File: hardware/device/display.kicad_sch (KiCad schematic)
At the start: 8 parts, among them U19 ER-TFT024IPS-3

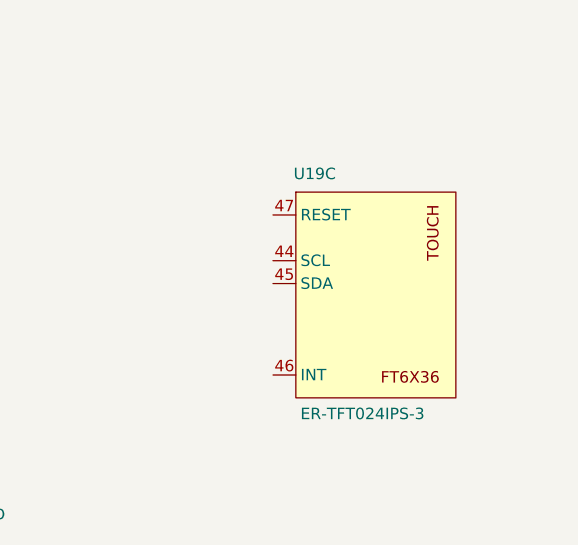
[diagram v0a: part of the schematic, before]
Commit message: feat: start codec layout
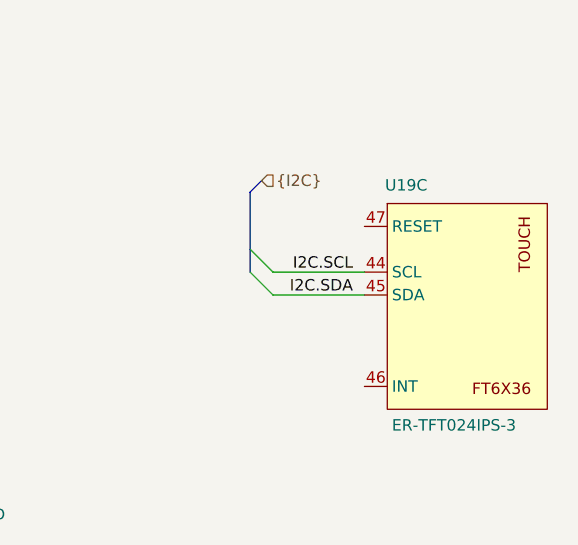
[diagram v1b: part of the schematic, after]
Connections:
- net I2C.SCL: now reaches U19.44 (SCL)
- net I2C.SDA: now reaches U19.45 (SDA)
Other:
- moved on the sheet: U19C
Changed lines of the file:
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@@
+	)
+	(bus_entry
+		(at 121.92 105.41)
+		(size -2.54 -2.54)
+		(stroke
+			(width 0)
+			(type default)
+		)
 	)
 	(bus_entry
@@
 	)
 	(bus_entry
+		(at 121.92 107.95)
+		(size -2.54 -2.54)
+		(stroke
+			(width 0)
+			(type default)
+		)
+	)
+	(bus_entry
 		(at 21.59 96.52)
 		(size -2.54 -2.54)
@@
 		)
 	)
+	(bus
+		(pts
+			(xy 119.38 96.52) (xy 119.38 102.87)
+		)
+		(stroke
+			(width 0)
+			(type default)
+		)
+	)
 	(wire
 		(pts
@@
 		)
 	)
+	(bus
+		(pts
+			(xy 119.38 102.87) (xy 119.38 105.41)
+		)
+		(stroke
+			(width 0)
+			(type default)
+		)
+	)
 	(wire
 		(pts
@@
 		)
 	)
+	(bus
+		(pts
+			(xy 119.38 96.52) (xy 120.65 95.25)
+		)
+		(stroke
+			(width 0)
+			(type default)
+		)
+	)
 	(wire
 		(pts
@@
 	(wire
 		(pts
+			(xy 121.92 105.41) (xy 132.08 105.41)
+		)
+		(stroke
+			(width 0)
+			(type default)
+		)
+	)
+	(wire
+		(pts
 			(xy 64.77 125.73) (xy 90.17 125.73)
 		)
@@
 		(pts
 			(xy 21.59 73.66) (xy 34.29 73.66)
+		)
+		(stroke
+			(width 0)
+			(type default)
+		)
+	)
+	(wire
+		(pts
+			(xy 121.92 107.95) (xy 132.08 107.95)
 		)
 		(stroke
@@
 		)
 	)
+	(label "I2C.SDA"
+		(at 130.81 107.95 180)
+		(effects
+			(font
+				(size 1.27 1.27)
+			)
+			(justify right bottom)
+		)
+	)
 	(label "FMC.D2"
 		(at 33.02 63.5 180)
@@
 		)
 	)
+	(label "I2C.SCL"
+		(at 130.81 105.41 180)
+		(effects
+			(font
+				(size 1.27 1.27)
+			)
+			(justify right bottom)
+		)
+	)
 	(label "FMC.NWE"
 		(at 33.02 111.76 180)
@@
 			)
 			(justify right bottom)
+		)
+	)
+	(hierarchical_label "{I2C}"
+		(shape input)
+		(at 120.65 95.25 0)
+		(effects
+			(font
+				(size 1.27 1.27)
+			)
+			(justify left)
 		)
 	)
@@
 	(symbol
 		(lib_id "pocket_synth:ER-TFT024IPS-3")
-		(at 133.35 107.95 0)
+		(at 143.51 109.22 0)
 		(unit 3)
 		(exclude_from_sim no)
@@
 		(dnp no)
 		(property "Reference" "U19"
-			(at 124.206 94.488 0)
+			(at 134.366 95.758 0)
 			(effects
 				(font
@@
 		)
 		(property "Value" "ER-TFT024IPS-3"
-			(at 124.968 121.158 0)
+			(at 135.128 122.428 0)
 			(effects
 				(font
@@
 		)
 		(property "Footprint" "pocket_synth:ER-TFT024IPS-3"
-			(at 133.35 107.95 0)
+			(at 143.51 109.22 0)
 			(effects
 				(font
@@
 		)
 		(property "Datasheet" ""
-			(at 133.35 107.95 0)
+			(at 143.51 109.22 0)
 			(effects
 				(font
@@
 		)
 		(property "Description" ""
-			(at 133.35 107.95 0)
+			(at 143.51 109.22 0)
 			(effects
 				(font
@@
 		)
 		(property "JLC" ""
-			(at 133.35 107.95 0)
-			(effects
-				(font
+			(at 143.51 109.22 0)
+			(effects
+				(font

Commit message: feat: various audio and power schematic layout
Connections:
- net GND: no longer U19.39 (TE)
- new net DISPLAY_TE: U19.39 (TE)
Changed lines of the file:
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@@
-	)
-	(junction
-		(at 90.17 93.98)
-		(diameter 0)
-		(color 0 0 0 0)
 	)
 	(junction
@@
 	(wire
 		(pts
-			(xy 90.17 77.47) (xy 90.17 93.98)
-		)
-		(stroke
-			(width 0)
-			(type default)
-		)
-	)
-	(wire
-		(pts
 			(xy 87.63 77.47) (xy 90.17 77.47)
 		)
@@
 	(wire
 		(pts
-			(xy 90.17 93.98) (xy 90.17 125.73)
+			(xy 90.17 77.47) (xy 90.17 125.73)
 		)
 		(stroke
@@
 	(wire
 		(pts
-			(xy 87.63 93.98) (xy 90.17 93.98)
+			(xy 87.63 93.98) (xy 92.71 93.98)
 		)
 		(stroke
@@
 		(effects
 			(font
+				(size 1.27 1.27)
+			)
+			(justify left)
+		)
+	)
+	(hierarchical_label "DISPLAY_TE"
+		(shape input)
+		(at 92.71 93.98 0)
+		(effects
+			(font

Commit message: chore: schematic organization
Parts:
- C4, C5, C6: footprint (none) -> Capacitor_SMD:C_0402_1005Metric
- R4, R5, R6, R7: footprint (none) -> Resistor_SMD:R_0402_1005Metric
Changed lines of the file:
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@@
 			)
 		)
-		(property "Footprint" ""
+		(property "Footprint" "Resistor_SMD:R_0402_1005Metric"
 			(at 115.57 61.468 90)
 			(effects
@@
 			)
 		)
-		(property "Footprint" ""
+		(property "Footprint" "Capacitor_SMD:C_0402_1005Metric"
 			(at 64.4652 35.56 0)
 			(effects
@@
 			)
 		)
-		(property "Footprint" ""
+		(property "Footprint" "Resistor_SMD:R_0402_1005Metric"
 			(at 115.57 57.658 90)
 			(effects
@@
 			)
 		)
-		(property "Footprint" ""
+		(property "Footprint" "Resistor_SMD:R_0402_1005Metric"
 			(at 115.57 65.278 90)
 			(effects
@@
 			)
 		)
-		(property "Footprint" ""
+		(property "Footprint" "Capacitor_SMD:C_0402_1005Metric"
 			(at 72.0852 35.56 0)
 			(effects
@@
 			)
 		)
-		(property "Footprint" ""
+		(property "Footprint" "Resistor_SMD:R_0402_1005Metric"
 			(at 115.57 69.088 90)
 			(effects
@@
 			)
 		)
-		(property "Footprint" ""
+		(property "Footprint" "Capacitor_SMD:C_0402_1005Metric"
 			(at 79.7052 35.56 0)
 			(effects

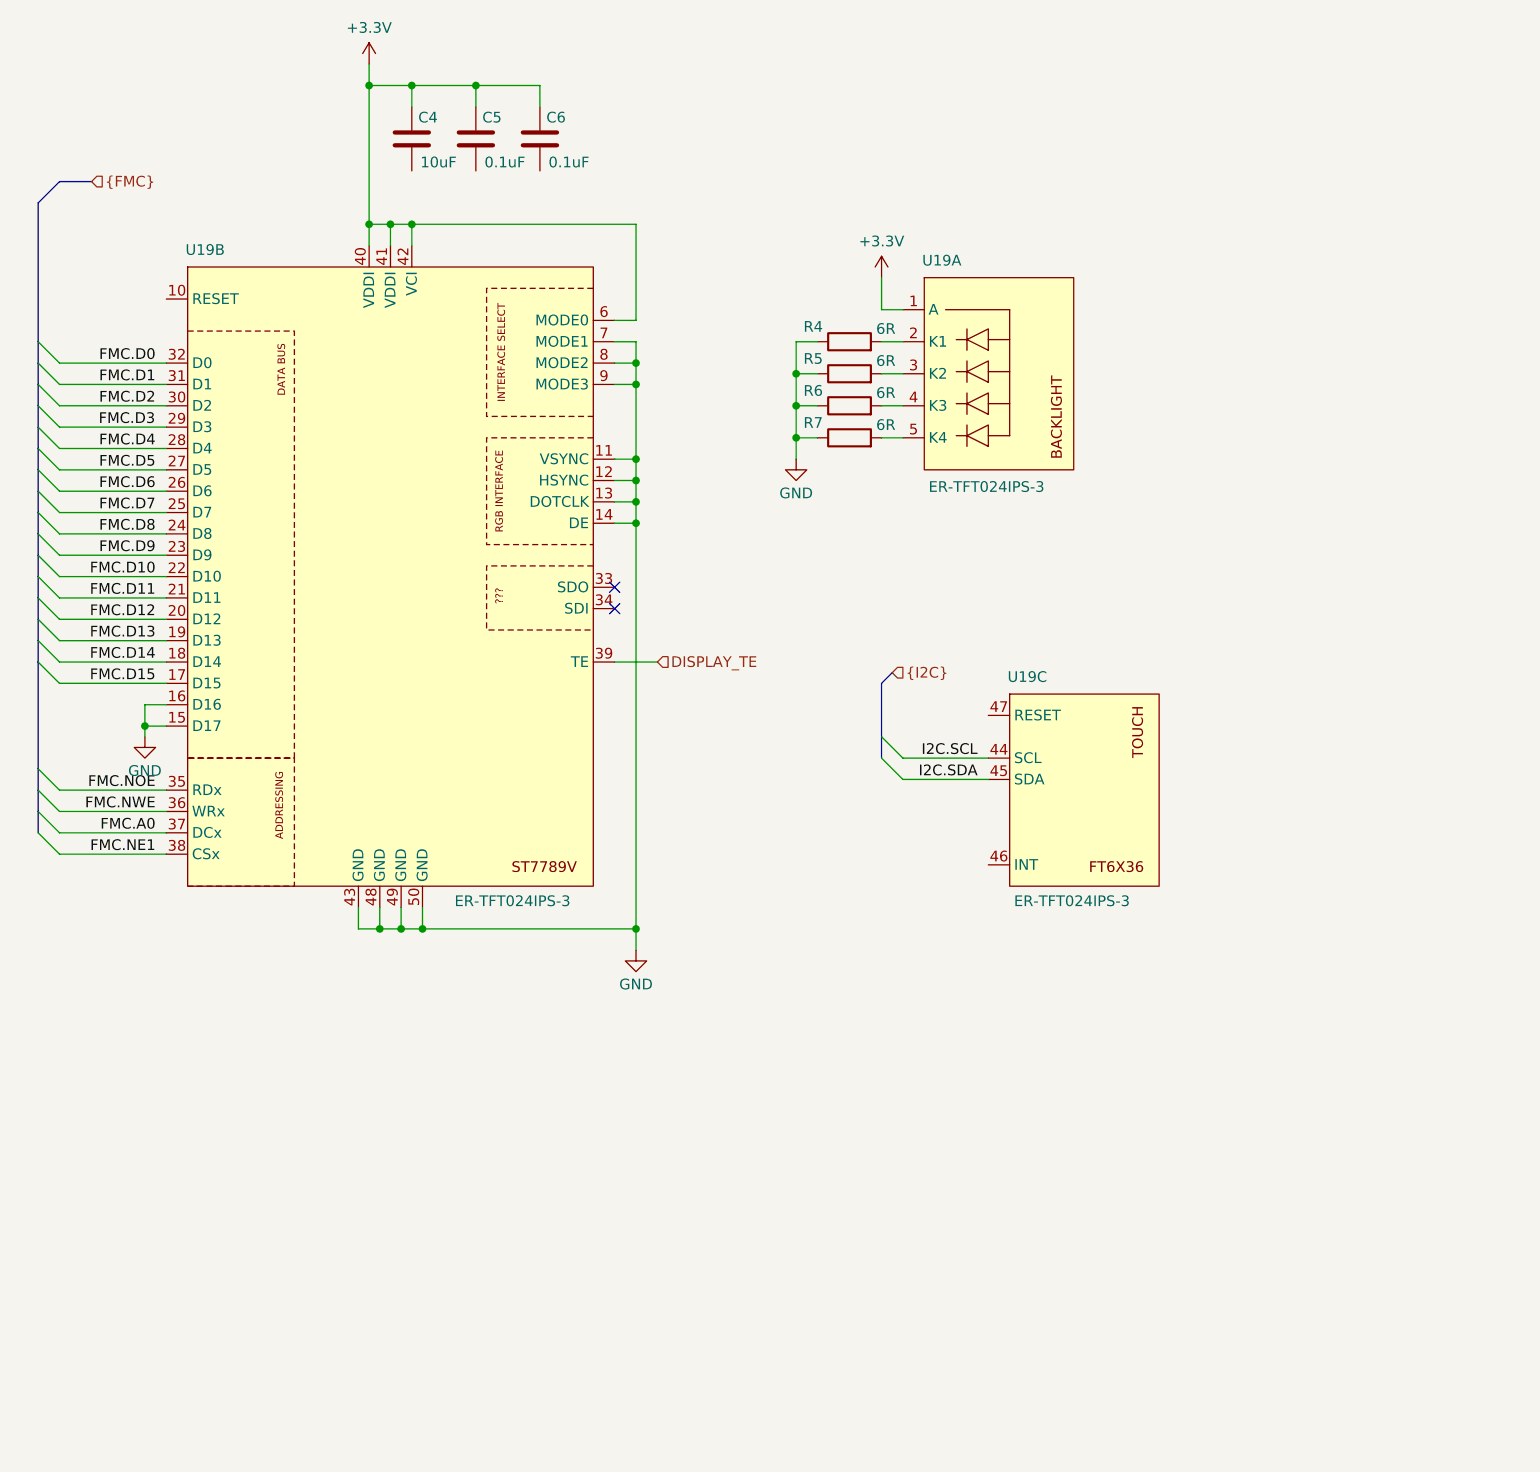
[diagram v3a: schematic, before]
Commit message: feat: various routing, footprint and schematic cleanup
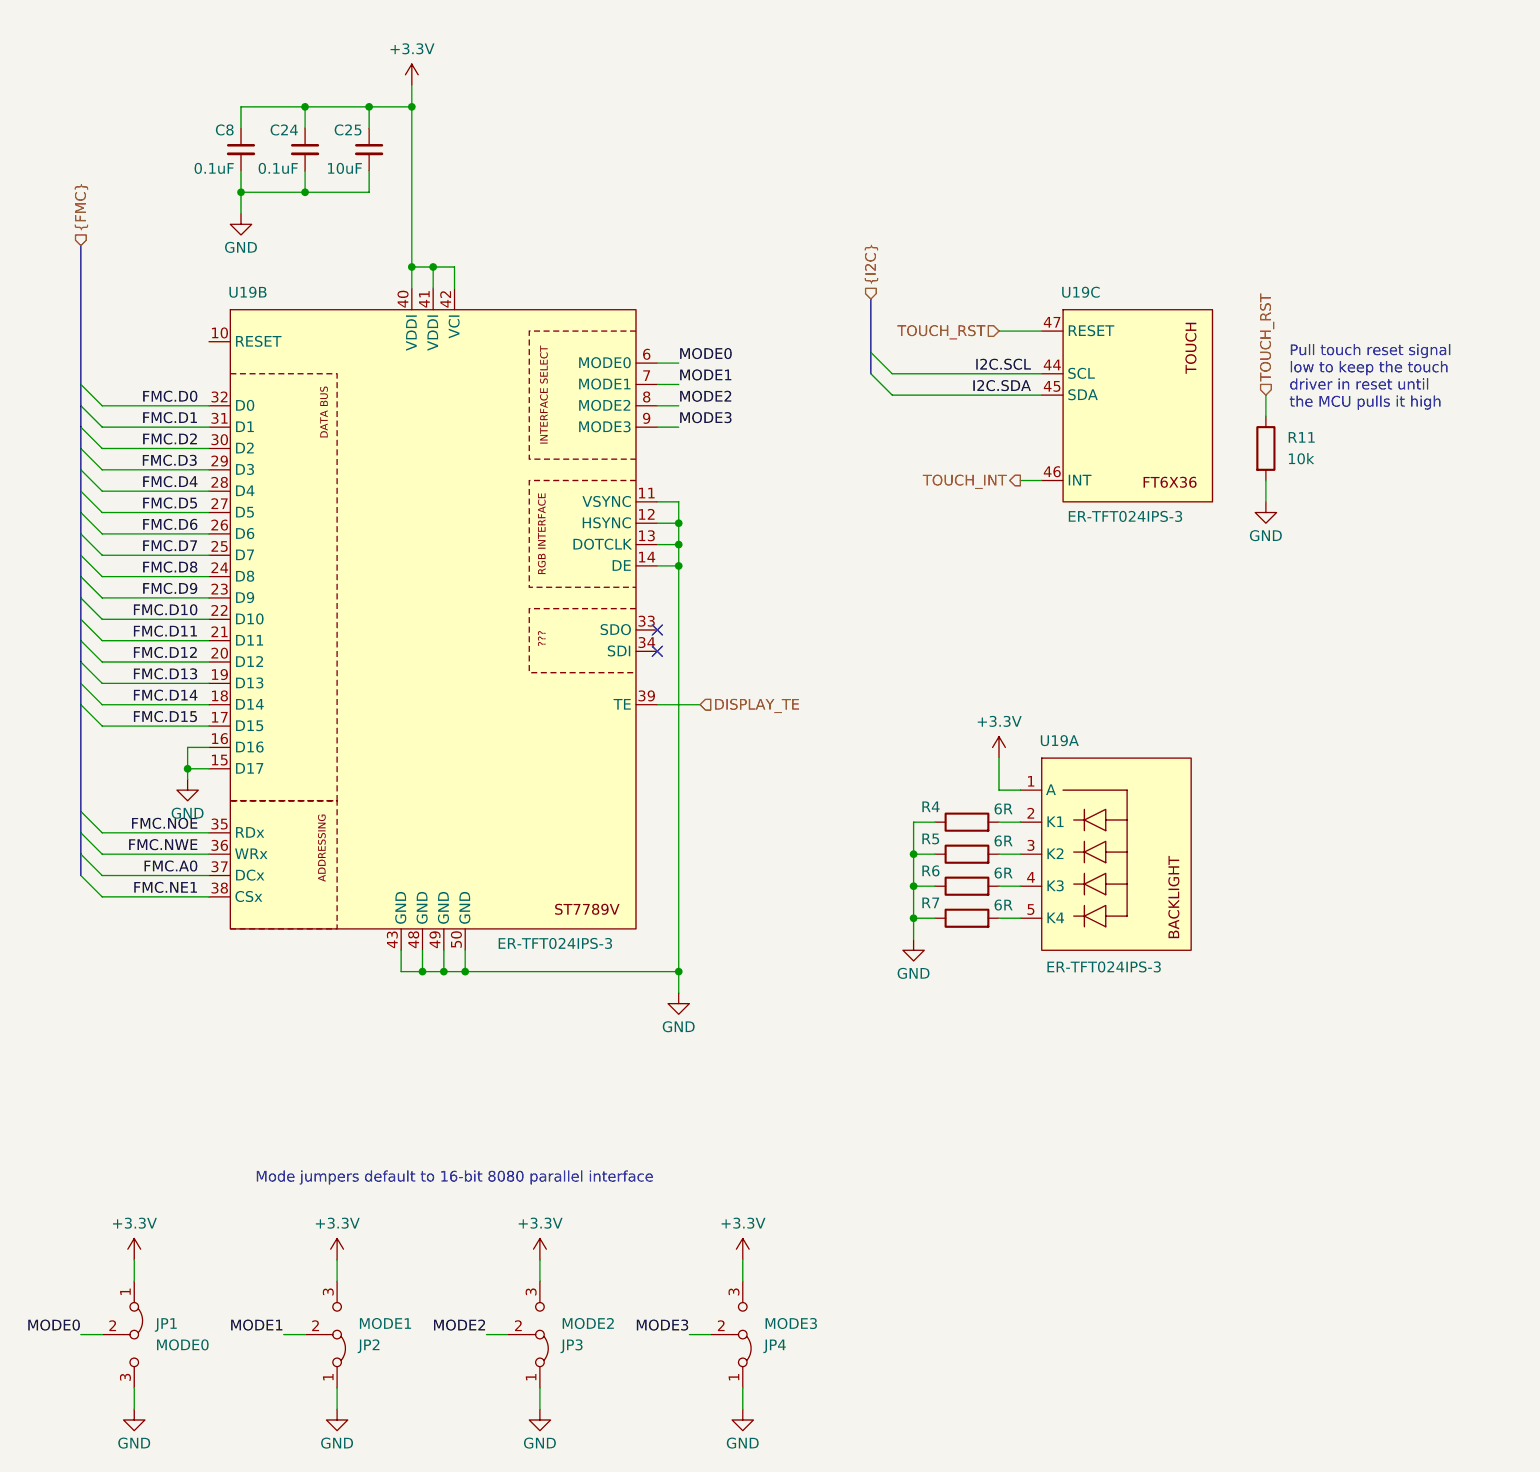
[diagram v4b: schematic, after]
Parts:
- removed C4: 10uF, Capacitor_SMD:C_0402_1005Metric, symbol Device:C
- removed C5, C6: 0.1uF, Capacitor_SMD:C_0402_1005Metric, symbol Device:C
- added C24, C8: 0.1uF, Capacitor_SMD:C_0402_1005Metric, symbol Device:C_Small
- added C25: 10uF, Capacitor_SMD:C_0402_1005Metric, symbol Device:C_Small
- added JP1: MODE0, Jumper:SolderJumper-3_P1.3mm_Bridged12_RoundedPad1.0x1.5mm, symbol Jumper:Jumper_3_Bridged12
- added JP2: MODE1, Jumper:SolderJumper-3_P1.3mm_Bridged12_RoundedPad1.0x1.5mm, symbol Jumper:Jumper_3_Bridged12
- added JP3: MODE2, Jumper:SolderJumper-3_P1.3mm_Bridged12_RoundedPad1.0x1.5mm, symbol Jumper:Jumper_3_Bridged12
- added JP4: MODE3, Jumper:SolderJumper-3_P1.3mm_Bridged12_RoundedPad1.0x1.5mm, symbol Jumper:Jumper_3_Bridged12
- added R11: 10k, Resistor_SMD:R_0402_1005Metric, symbol Device:R
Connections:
- net +3.3V: now also C24.1, C25.1, C8.1, JP1.1 (A), JP2.3 (B), JP3.3 (B), JP4.3 (B); no longer U19.6 (MODE0)
- net GND: now also C24.2, C25.2, C8.2, JP1.3 (B), JP2.1 (A), JP3.1 (A), JP4.1 (A), R11.2; no longer U19.7 (MODE1), U19.8 (MODE2), U19.9 (MODE3)
- net TOUCH_INT: now reaches U19.46 (INT)
- net TOUCH_RST: now reaches U19.47 (RESET)
- net TOUCH_RST: now also R11.1
- new net MODE0: JP1.2 (C), U19.6 (MODE0)
- new net MODE1: JP2.2 (C), U19.7 (MODE1)
- new net MODE2: JP3.2 (C), U19.8 (MODE2)
- new net MODE3: JP4.2 (C), U19.9 (MODE3)
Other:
- note added: "Mode jumpers default to 16-bit 8080 parallel interface"
- note added: "Pull touch reset signal low to keep the touch driver in reset until the MCU pulls it high"
- moved on the sheet: R4, R5, R6, R7, U19A, U19B, U19C
